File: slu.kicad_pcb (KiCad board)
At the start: 2 copper layers, 99.6 x 100.9 mm, 168 parts, among them J1 lcd_out, sw1 sw_2pos

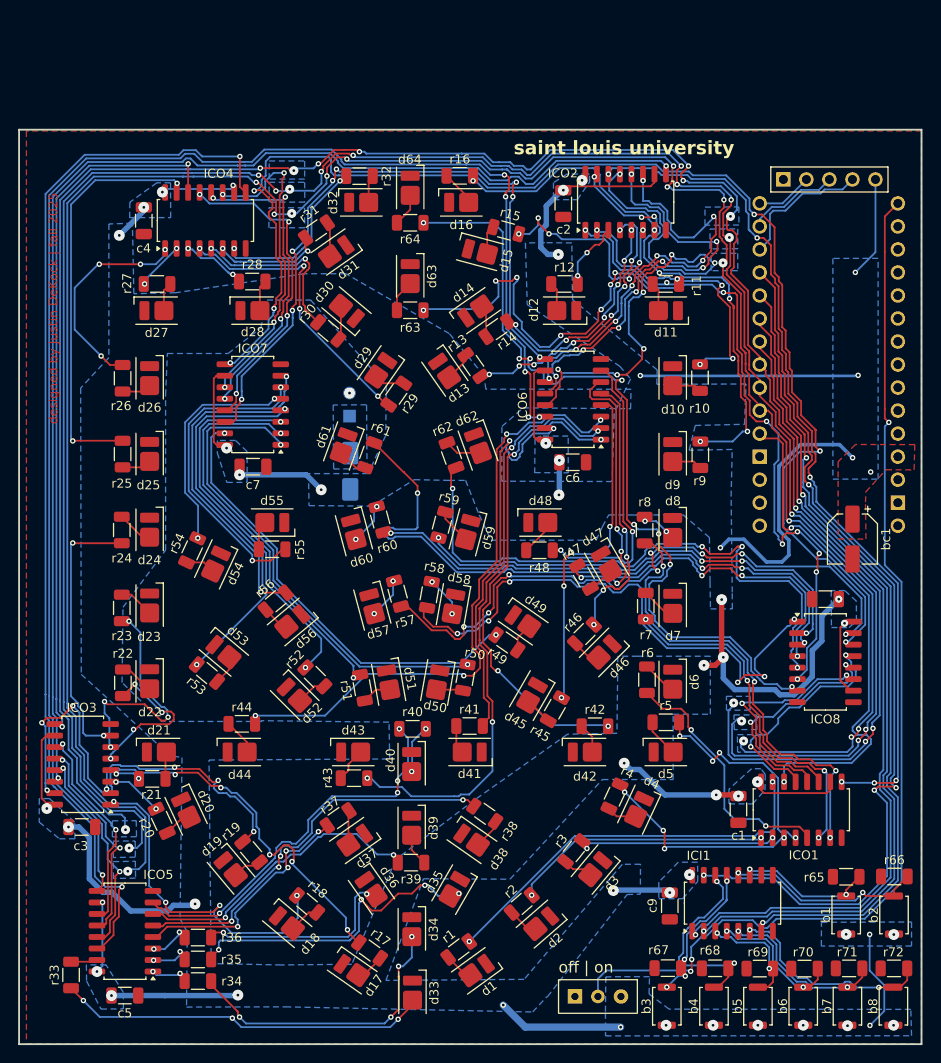
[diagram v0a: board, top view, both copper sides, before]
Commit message: project name engraving added take 2
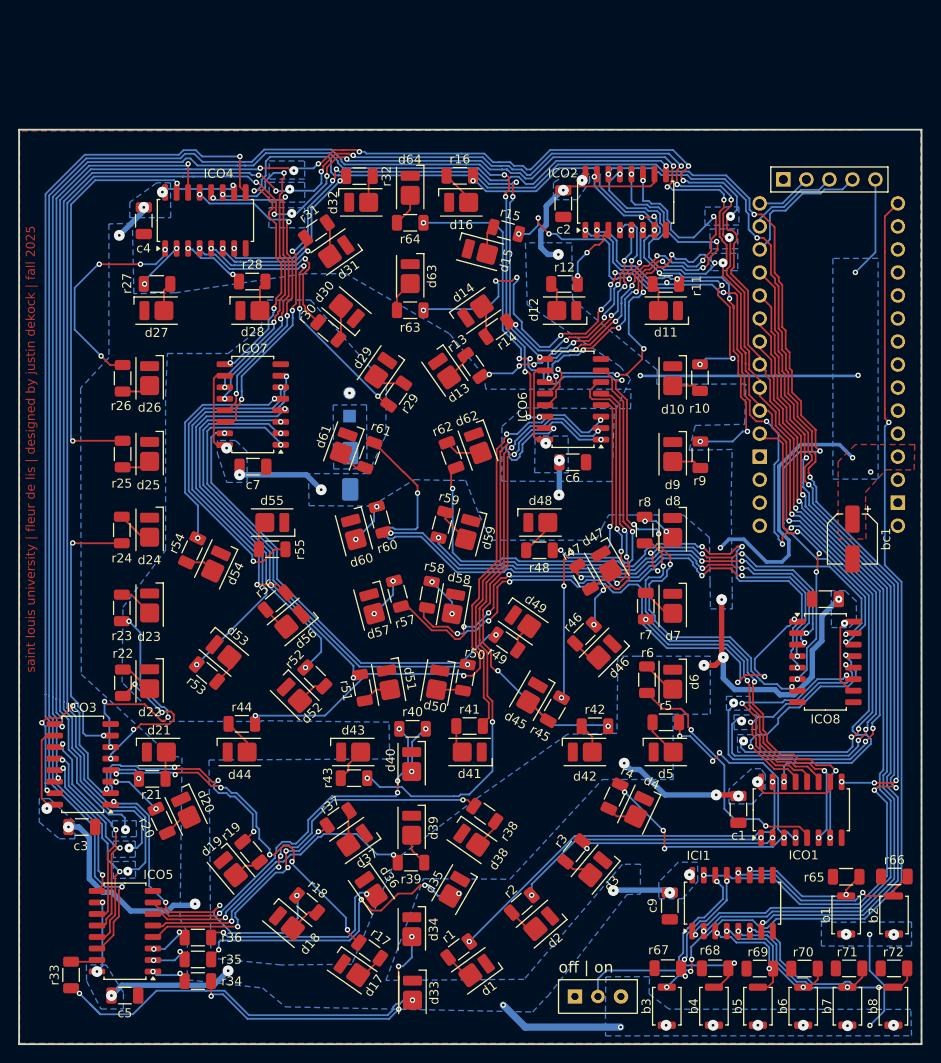
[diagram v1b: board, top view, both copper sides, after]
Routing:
- net Net-(d33-A): track 41.0 -> 43.0 mm, vias 3 -> 2
- net Net-(d34-A): track 34.1 -> 35.0 mm
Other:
- board text added: "saint louis university | fleur de lis | designed by justin dekock | fall 2025"
- board text removed: "designed by Justin DeKock | fall 2025"
- board text removed: "saint louis university"

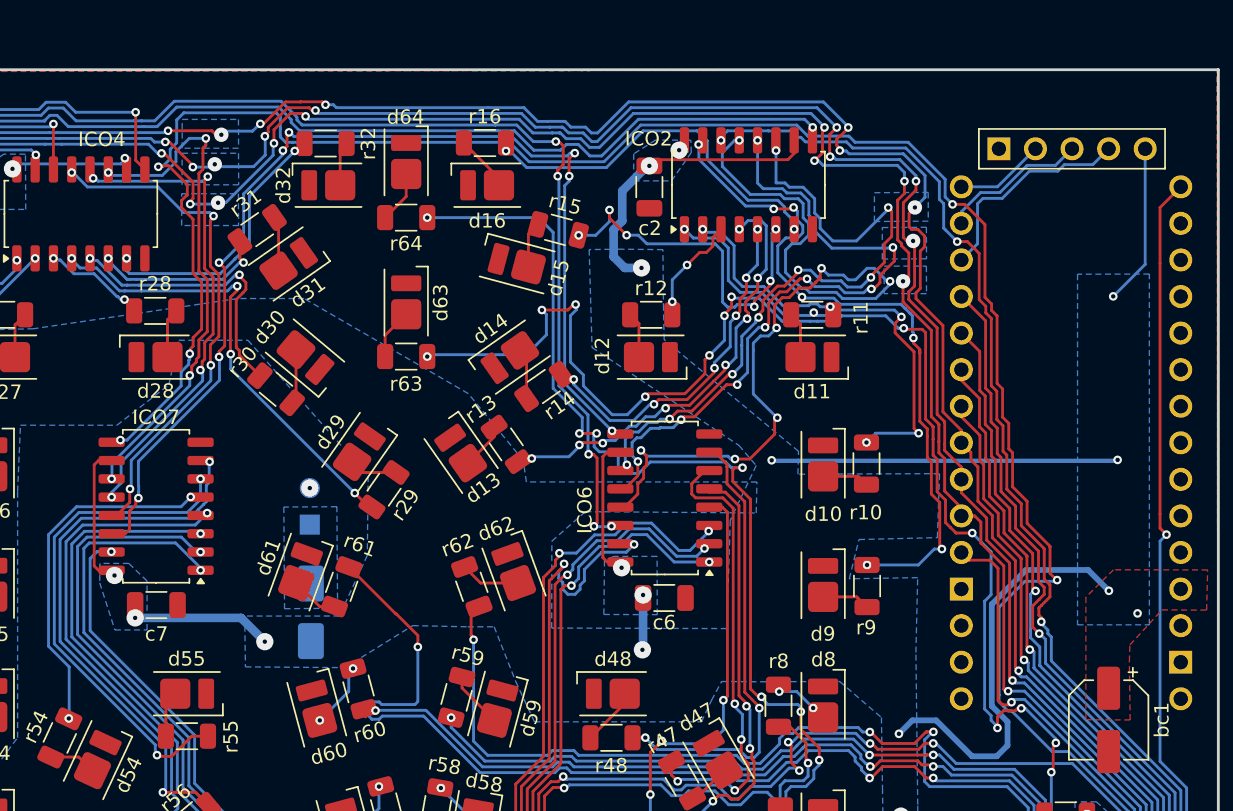
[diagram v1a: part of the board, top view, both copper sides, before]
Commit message: added back silkscreen labels
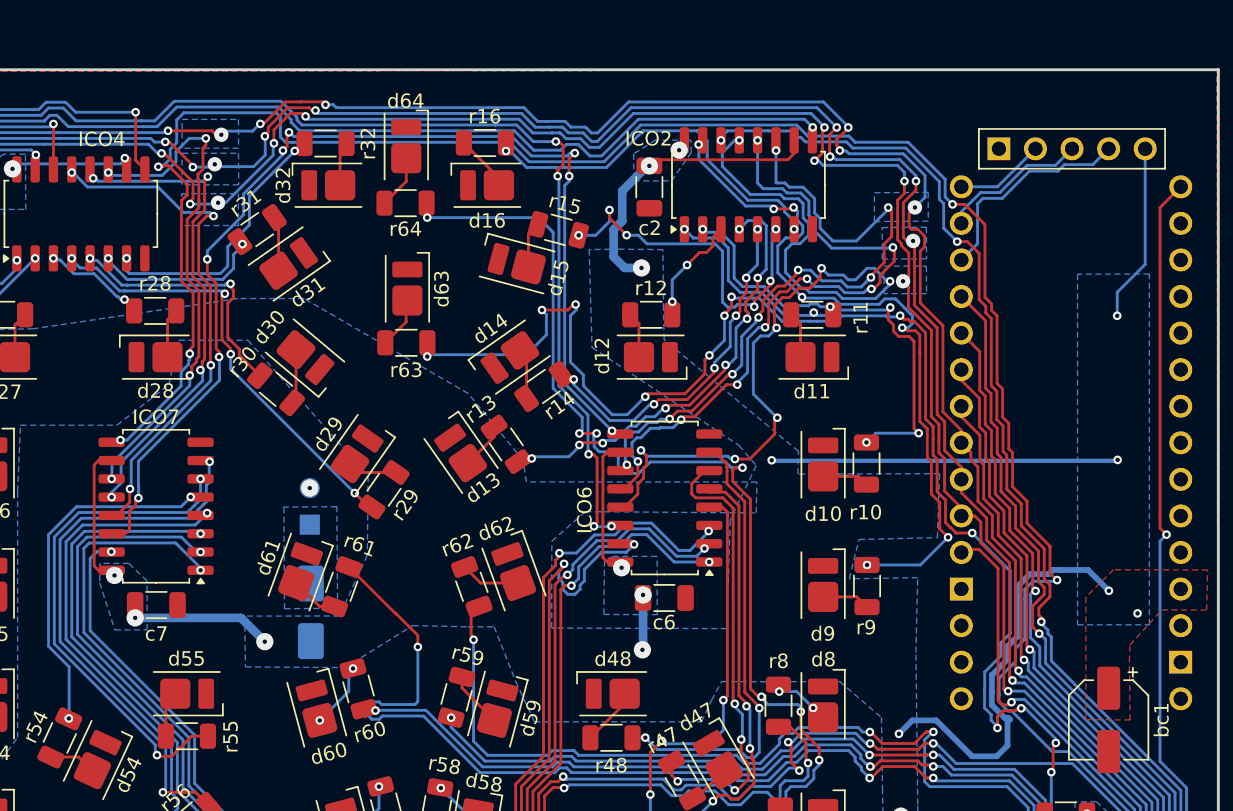
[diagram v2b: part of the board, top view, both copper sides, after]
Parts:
- moved d64 1.10 mm to (100.1, 53.4)
- moved r64 1.01 mm to (100.0, 57.4)
- moved d63 0.96 mm to (100.2, 63.3)
- moved r63 0.96 mm to (100.1, 67.1)
- moved d29 0.21 mm to (96.7, 74.8)
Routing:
- net /ICD9: track 48.6 -> 50.3 mm
- net /ICD30: track 20.2 -> 18.5 mm
- net /ICD29: track 32.4 -> 31.1 mm
- net /ICD63: track 103.2 -> 104.4 mm
- net +5V: track 288.8 -> 290.0 mm
- net Net-(d63-A): track 3.55 -> 4.45 mm
- net /SER7-8: track 147.5 -> 146.7 mm
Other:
- board text added: "5V"
- board text added: "EXT. LCD"
- board text added: "GND"
- board text added: "ce"
- board text added: "clk"
- board text added: "cp"
- board text added: "latch"
- board text added: "lch"
- board text added: "oe"
- board text added: "pl"
- board text added: "pwr"
- board text added: "ser"
- board text added: "serout"

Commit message: "major finishing touches"
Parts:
- moved r28 0.20 mm to (82.5, 64.8)
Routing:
- net /CLOCK: track 379.7 -> 396.6 mm
- net /LATCH: track 382.5 -> 397.7 mm, vias 30 -> 31
- net /ICD42: track 53.4 -> 58.8 mm, vias 4 -> 6
- net /ICD44: track 68.9 -> 72.5 mm, vias 4 -> 6
- net /ICD43: track 66.2 -> 69.5 mm, vias 4 -> 6
- net /ICD49: track 49.9 -> 53.2 mm
- net /ICD58: track 62.9 -> 59.6 mm, vias 6 -> 4
- net /ICD23: track 26.4 -> 23.3 mm
- net /ICD22: track 17.9 -> 15.4 mm, vias 4 -> 2
- net /ICD39: track 31.7 -> 34.1 mm
- net /ICD31: track 11.9 -> 14.2 mm
- net /ICD61: track 75.5 -> 73.3 mm
- net +5V: track 290.0 -> 292.1 mm, vias 50 -> 49
- net /ICD41: track 43.1 -> 45.1 mm, vias 2 -> 6
- net /ICD59: track 52.3 -> 50.4 mm
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
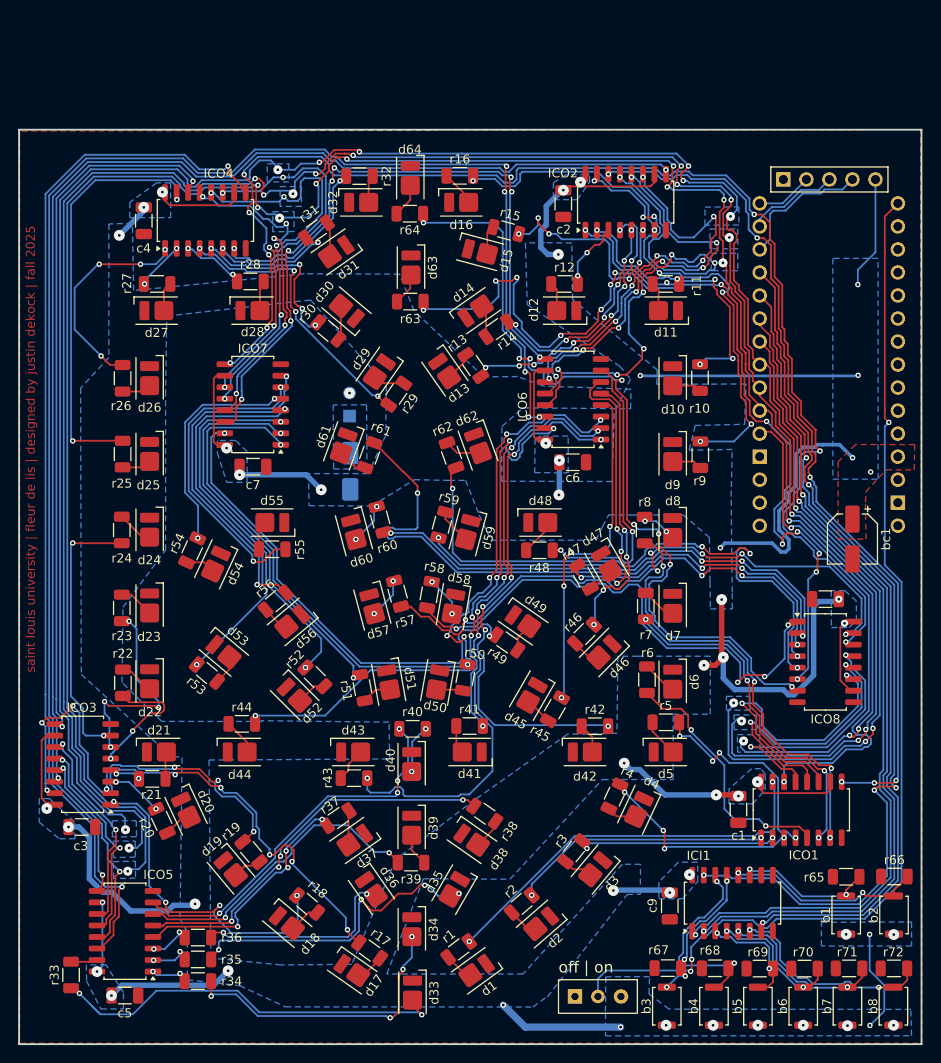
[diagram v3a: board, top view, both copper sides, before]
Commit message: added mount holes for battery
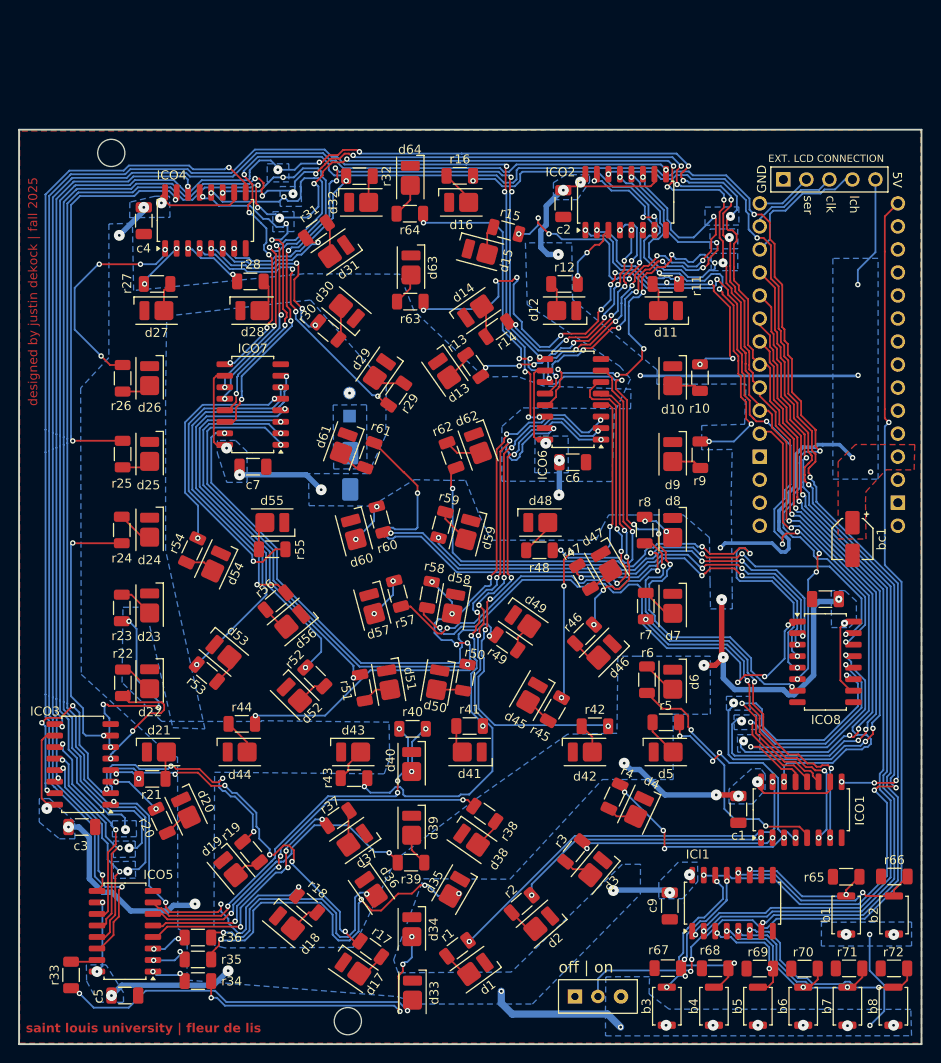
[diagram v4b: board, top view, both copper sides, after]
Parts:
- added REF**: MountingHole_3mm, slu_leds_lib:MountingHole_3mm, B.Cu at (93.2, 146.5)
- added REF**: MountingHole_3mm, slu_leds_lib:MountingHole_3mm, B.Cu at (67.1, 50.7)
- bc1: footprint slu_leds_lib:bulkcap_smd -> slu_leds_lib:CP_Elec_4x5.4
- moved d17 0.20 mm to (93.8, 140.8)
- moved r17 0.20 mm to (95.7, 138.5)
- moved d1 0.19 mm to (107.2, 140.8)
- moved r1 0.19 mm to (105.3, 138.4)
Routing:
- net Net-(d35-A): track 35.6 -> 42.1 mm
- net Net-(d36-A): track 22.2 -> 28.4 mm
- net Net-(d33-A): track 44.2 -> 39.1 mm
- net +5V: track 292.1 -> 294.7 mm
- net /SER3-4: track 77.5 -> 75.5 mm
- net /ICD25: track 46.3 -> 44.4 mm
- net /ICD44: track 72.5 -> 74.1 mm
- net Net-(d28-A): track 4.83 -> 6.15 mm
- net /LATCH: track 397.7 -> 396.4 mm
- net /ICD43: track 69.5 -> 68.4 mm
- net /SER4-5: track 115.7 -> 114.5 mm
- net /ICD9: track 50.1 -> 49.0 mm
- net /SER5-6: track 164.6 -> 163.5 mm
- net /SER2-3: track 137.8 -> 136.8 mm
- net /CLOCK: track 396.6 -> 395.6 mm
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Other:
- board text added: "EXT. LCD CONNECTION"
- board text added: "designed by justin dekock | fall 2025"
- board text added: "pwr sw (d13)"
- board text added: "saint louis university | fleur de lis"
- board text added: "source code: https://github.com/jdetok/slu_leds_c"
- board text removed: "EXT. LCD"
- board text removed: "pwr"
- board text removed: "saint louis university | fleur de lis | designed by justin dekock | fall 2025"
